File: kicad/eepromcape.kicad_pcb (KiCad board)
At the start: 2 copper layers, 33 x 22.9 mm, 5 parts, among them J1 Conn_01x12, J2 Conn_01x12, J3 Conn_02x04_Counter_Clockwise

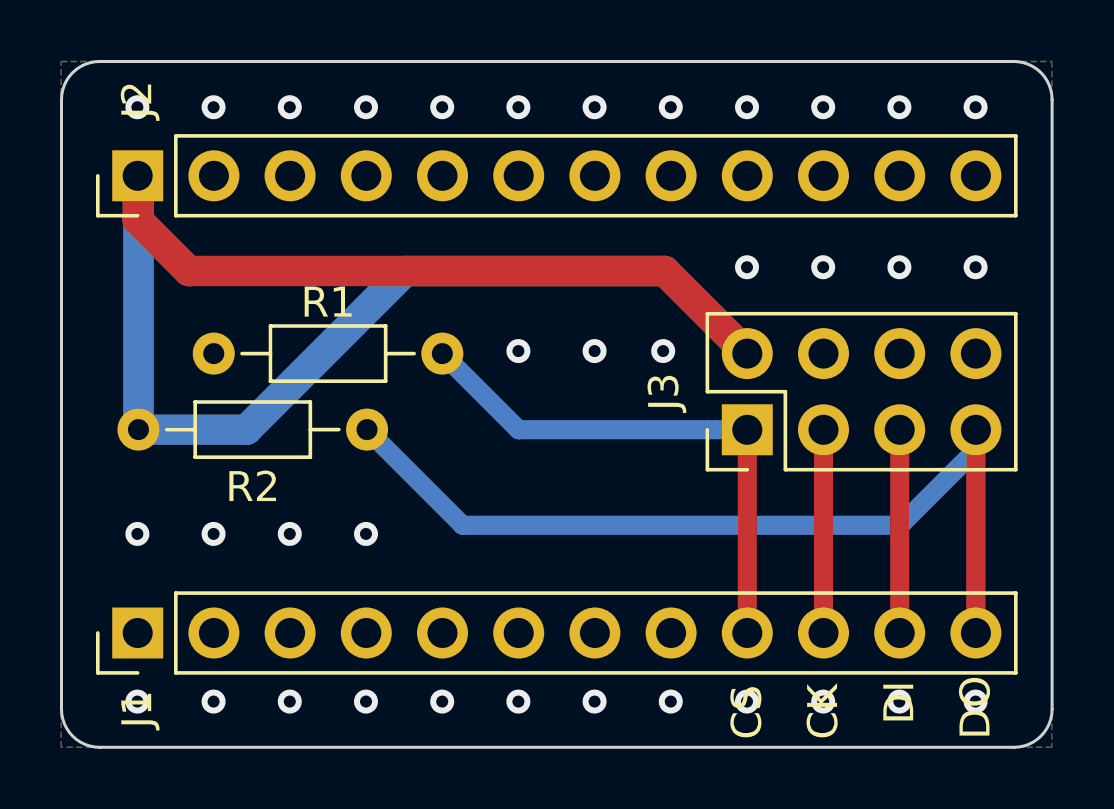
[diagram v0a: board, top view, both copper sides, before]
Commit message: Remove superfluous power traces
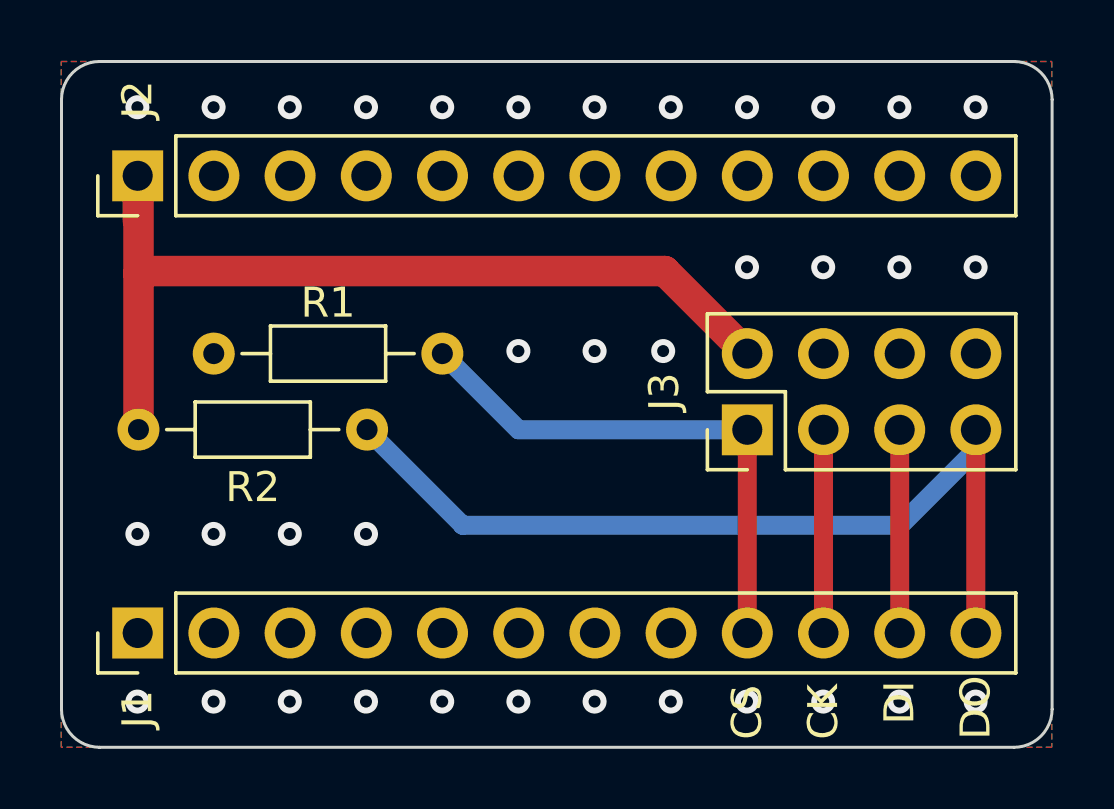
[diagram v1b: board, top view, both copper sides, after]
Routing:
- net +3V3: track 55.8 -> 31.5 mm
